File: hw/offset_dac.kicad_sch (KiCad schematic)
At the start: 37 parts, among them Q1 SSM6N35AFE, Q3 SSM6N35AFE, U22 TSV992A, U23 MCP47CVB02-E_UN

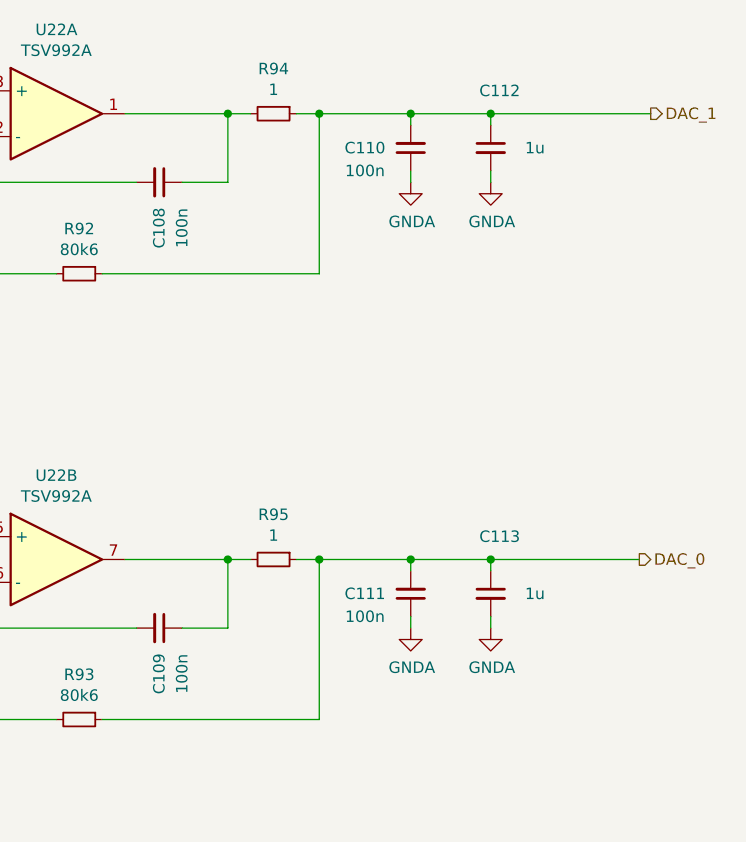
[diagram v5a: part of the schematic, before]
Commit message: removed buffer and 100n DAC output caps
 - prep for updating PCB to remove buffer stuff
 - caps were moved to buffer (close to switch)
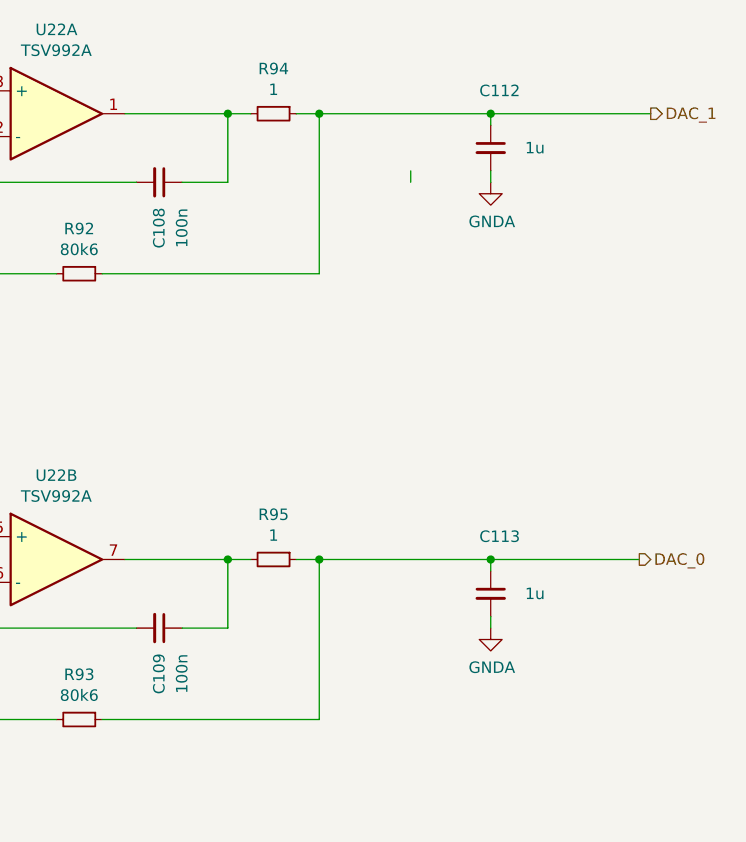
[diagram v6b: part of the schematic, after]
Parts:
- removed C110, C111: 100n, Capacitor_SMD:C_0603_1608Metric, symbol Device:C_Small

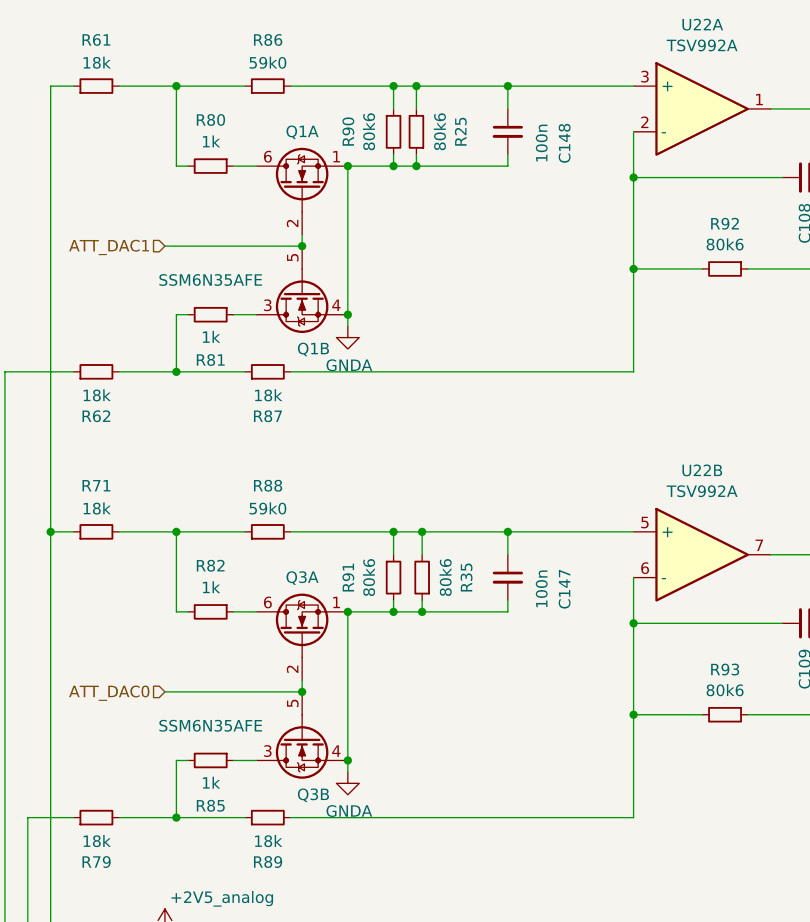
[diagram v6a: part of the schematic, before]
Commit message: added pll clock in divider from BNC, several pull-resistors
pull-resistors permit distinguishing board revisions.
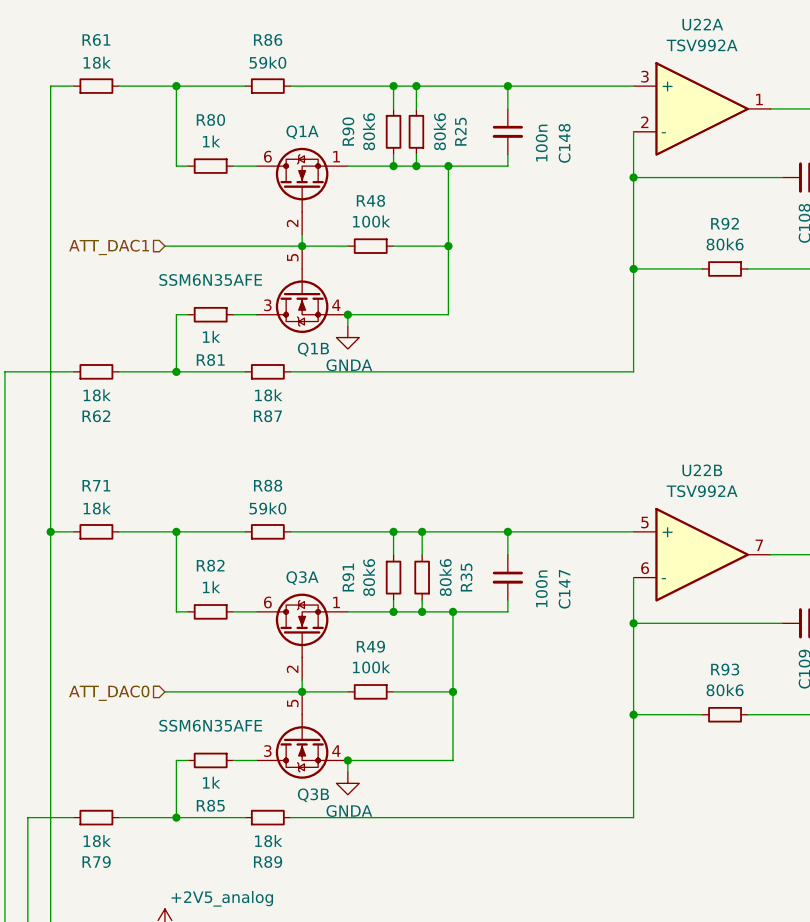
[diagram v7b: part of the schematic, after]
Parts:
- added R48, R49: 100k, Resistor_SMD:R_0603_1608Metric, symbol Device:R_Small
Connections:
- net ATT_DAC0: now also R49.2
- net ATT_DAC1: now also R48.2
- net GNDA: now also R48.1, R49.1

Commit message: updated parts assignments
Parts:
- R25, R35, R90, R91, R92, R93: Manufacturer (none) -> Stackpole; Part (none) -> RMCF0603FT80K6
- R48, R49: Manufacturer (none) -> Stackpole; Part (none) -> RMCF0603FT100K
- R61, R62, R71, R79, R87, R89: Manufacturer (none) -> Stackpole; Part (none) -> RMCF0603FT18K0
- R80, R81, R82, R85: Manufacturer (none) -> Stackpole; Part (none) -> RMCF0603FT1K00
- R86, R88: Manufacturer (none) -> Stackpole; Part (none) -> RMCF0603FT59K0
- R94, R95: Manufacturer (none) -> Stackpole; Part (none) -> RMCF0603FT1R00
